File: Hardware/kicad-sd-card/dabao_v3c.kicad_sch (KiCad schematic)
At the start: 42 parts, among them J1 USB_A, SW1 SW_Push, U1 EMS4000RSW, U2 baochip1x, U3 MT3406, U4 MT3406, Y1 48.000MHz

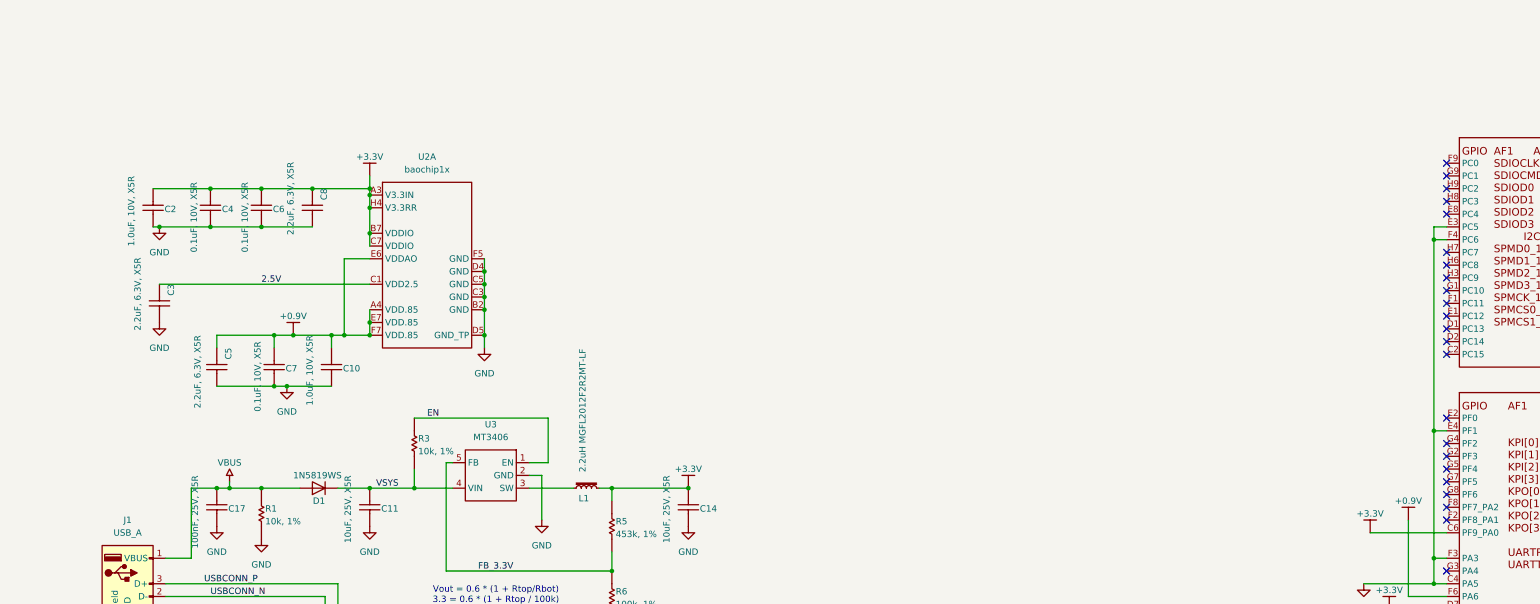
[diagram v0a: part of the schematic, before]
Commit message: Hardware: move KiCad project into kicad-sd-card/
Relocate dabao_v3c board, Library.pretty, gerbers, production, docs/pinout.
Add .gitignore for fp-info-cache, KiCad backups, lock files.
Remove nested .git from working copy so tree is tracked by main repo.

Made-with: Cursor
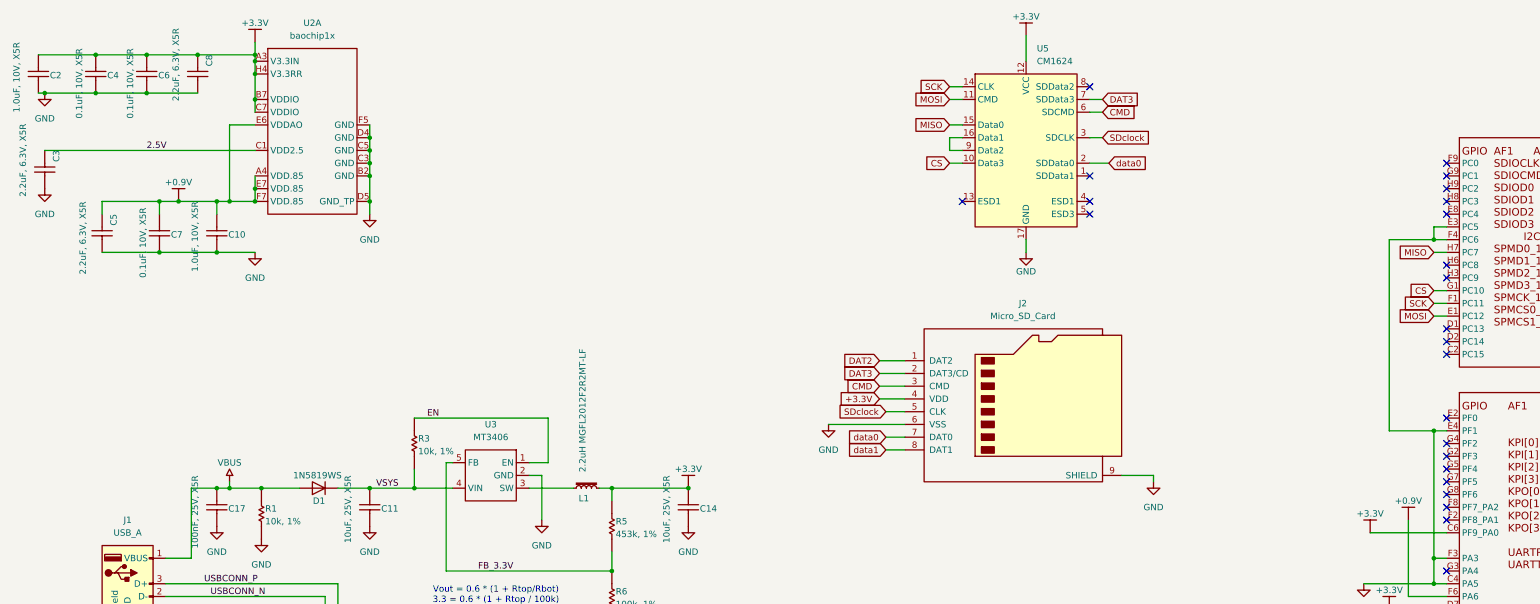
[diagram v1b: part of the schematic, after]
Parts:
- added J2: Micro_SD_Card, Connector_Card:microSD_HC_Hirose_DM3AT-SF-PEJM5, symbol Connector:Micro_SD_Card
- added U5: CM1624, Package_DFN_QFN:OnSemi_UDFN-16-1EP_1.35x3.3mm_P0.4mm_EP0.4x2.8mm, symbol Power_Protection:CM1624
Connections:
- net +3.3V: now also J2.4 (VDD), U5.12 (VCC)
- net GND: now also J2.6 (VSS), J2.9 (SHIELD), U5.17 (GND)
- net MOSI: now reaches U2.E1 (PC12)
- net MOSI: now also U5.11 (CMD)
- net SCK: now reaches U2.F1 (PC11)
- net SCK: now also U5.14 (CLK)
- net CS: now reaches U2.G1 (PC10)
- net CS: now also U5.10 (Data3)
- net MISO: now reaches U2.H7 (PC7)
- net MISO: now also U5.15 (Data0)
- new net: U5.16 (Data1), U5.9 (Data2)
- new net CMD: J2.3 (CMD), U5.6 (SDCMD)
- new net DAT2: J2.1 (DAT2)
- new net DAT3: J2.2 (DAT3/CD), U5.7 (SDData3)
- new net SDclock: J2.5 (CLK), U5.3 (SDCLK)
- new net data0: J2.7 (DAT0), U5.2 (SDData0)
- new net data1: J2.8 (DAT1)
- no-connect marks 41 -> 42
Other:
- moved on the sheet: C10, C2, C3, C4, C5, C6, C7, C8, U2A
